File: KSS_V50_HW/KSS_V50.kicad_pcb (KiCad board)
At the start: 4 copper layers, 159 x 21.7 mm, 128 parts, among them J1 Conn_01x02_Socket, J2 Conn_01x04_Socket, J3 Conn_01x04_Socket, J4 Conn_01x02_Socket, J5 Conn_01x04_Pin, J6 Conn_01x04_Pin, Q1 DMG3414U-7, Q2 DMG3414U-7, Q5 DMG3414U-7, Q6 SSM3J332R,LF, SW2 SW_SP3T, U1 SPV1040, U10 ATtiny3226-X, U11 AT42QT1010-TSHR, U12 SN74AUP1T34DCK, U13 SN74AUP1T34DCK, U14 SN74AUP1T34DCK, U15 SN74AUP1T34DCK, U2 INA236, U3 BQ29737, U4 INA236, U5 TPS62843, U6 TMAG5328, U7 TMC2300-LA-T, U8 TMAG5328, U9 TMC2300-LA-T

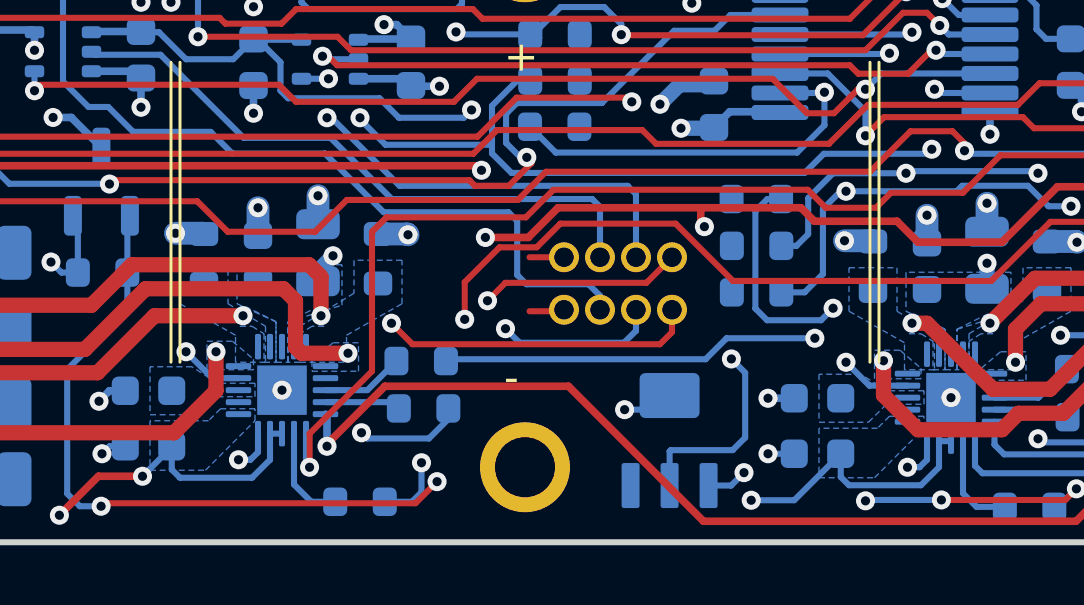
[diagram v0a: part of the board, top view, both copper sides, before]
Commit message: minor changed based on Wilson's first review and personal layout round
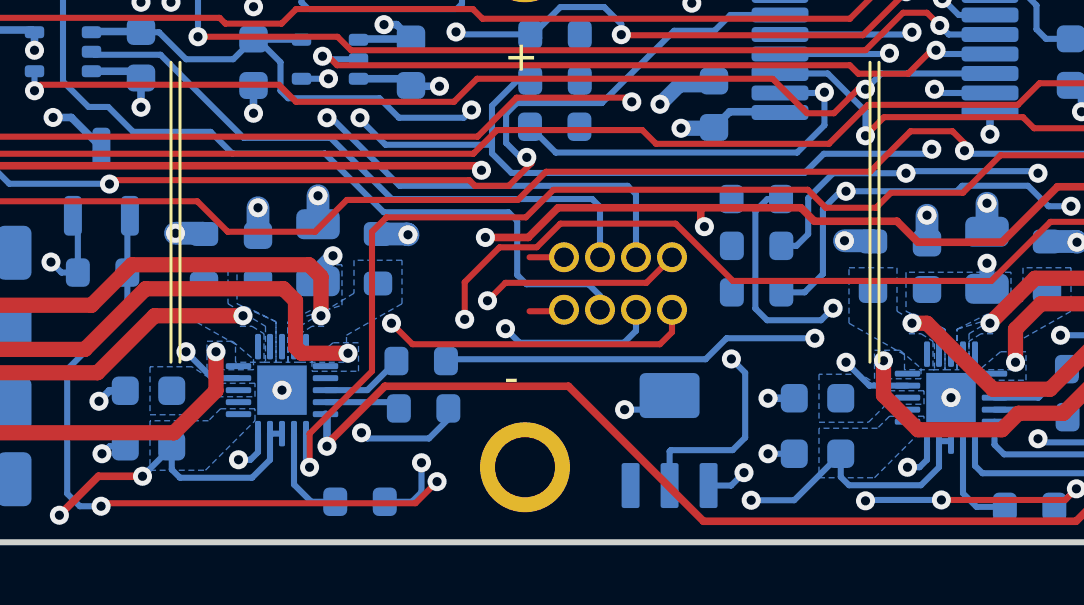
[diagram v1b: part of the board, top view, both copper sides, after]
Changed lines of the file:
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@@
 		)
 		(property "Value" "SN74AUP1T34DCK"
-			(at 0 -2 360)
+			(at 0 -2 0)
 			(layer "B.Fab")
 			(effects
@@
 		)
 		(property "Value" "47 uF"
-			(at 0 -1.85 360)
+			(at 0 -1.85 0)
 			(layer "B.Fab")
 			(effects
@@
 		)
 		(fp_text user "${REFERENCE}"
-			(at 0 0 360)
+			(at 0 0 0)
 			(layer "B.Fab")
 			(effects
@@
 		)
 		(property "Value" "47 uF"
-			(at 0 -1.85 360)
+			(at 0 -1.85 0)
 			(layer "B.Fab")
 			(effects
@@
 		)
 		(fp_text user "${REFERENCE}"
-			(at 0 0 360)
+			(at 0 0 0)
 			(layer "B.Fab")
 			(effects
@@
 		(tags "capacitor")
 		(property "Reference" "C4"
-			(at 0.65 -3.37 360)
+			(at 0.65 -3.37 0)
 			(layer "B.SilkS")
 			(effects
@@
 		)
 		(property "Value" "47 uF"
-			(at 0 -1.85 360)
+			(at 0 -1.85 0)
 			(layer "B.Fab")
 			(effects
@@
 		)
 		(fp_text user "${REFERENCE}"
-			(at 0 0 360)
+			(at 0 0 0)
 			(layer "B.Fab")
 			(effects
@@
 		)
 		(property "Value" "SN74AUP1T34DCK"
-			(at 0 -2 360)
+			(at 0 -2 0)
 			(layer "B.Fab")
 			(effects
@@
 		)
 		(property "Value" "SN74AUP1T34DCK"
-			(at 0 -2 360)
+			(at 0 -2 0)
 			(layer "B.Fab")
 			(effects
@@
 		(tags "capacitor")
 		(property "Reference" "C1"
-			(at 0.625 -9.545 360)
+			(at 0.625 -9.545 0)
 			(layer "B.SilkS")
 			(effects
@@
 		)
 		(property "Value" "47 uF"
-			(at 0 -1.85 360)
+			(at 0 -1.85 0)
 			(layer "B.Fab")
 			(effects
@@
 		)
 		(fp_text user "${REFERENCE}"
-			(at 0 0 360)
+			(at 0 0 0)
 			(layer "B.Fab")
 			(effects
@@
 		)
 		(property "Value" "SN74AUP1T34DCK"
-			(at 0 -2 360)
+			(at 0 -2 0)
 			(layer "B.Fab")
 			(effects
@@
 		(filled_areas_thickness no)
 		(fill yes
-			(thermal_gap 0.5)
+			(thermal_gap 0.2)
 			(thermal_bridge_width 0.5)
 		)
@@
 			(pts
 				(xy 161 102.25) (xy 162.6 102.25) (xy 162.6 103.7) (xy 163.85 104.45) (xy 163.85 105.65) (xy 162.85 105.65)
-				(xy 162.85 104.75) (xy 161 103.7)
+				(xy 162.85 105.15) (xy 161 104.1)
 			)
 		)
@@
 			(pts
 				(xy 138.7 102) (xy 140.3 102) (xy 140.3 103.45) (xy 141.55 104.2) (xy 141.55 105.4) (xy 140.55 105.4)
-				(xy 140.55 104.5) (xy 138.7 103.45)
+				(xy 140.55 104.8) (xy 138.7 103.75)
 			)
 		)
